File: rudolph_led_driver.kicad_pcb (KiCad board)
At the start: 2 copper layers, 96 x 23 mm, 33 parts, among them J1 Conn_01x02_Female, J2 USB_B_Micro, J3 Conn_01x02_Male, Q1 S8050, Q2 2SC1815, Q3 2SC1815, Q4 S8050, Q5 S8050, Q6 2SC1815, SW1 ON/OFF, U1 LM809, U2 LP2980-ADJ, U3 MCP73831-2-OT

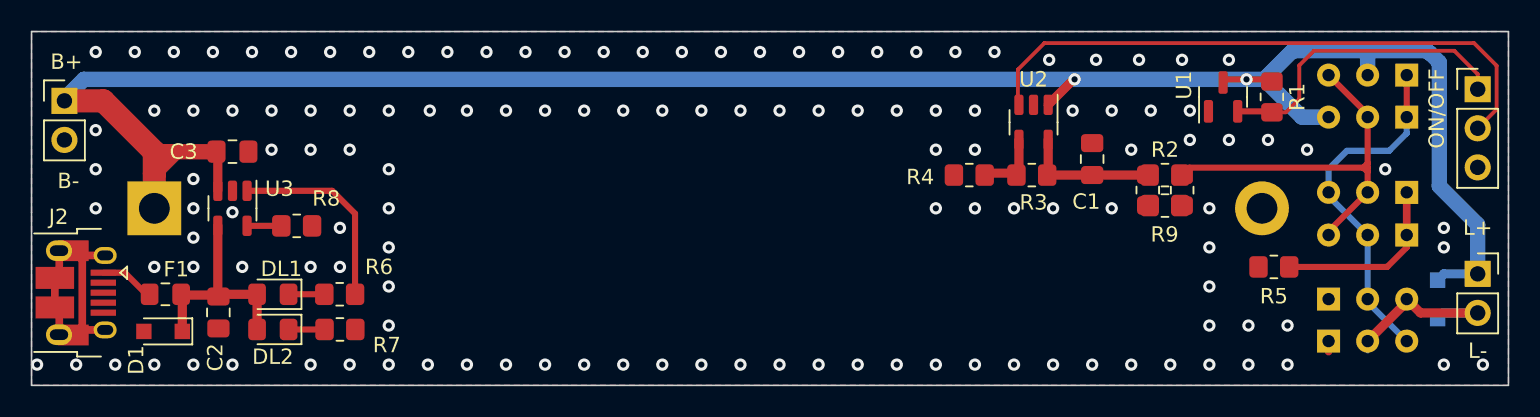
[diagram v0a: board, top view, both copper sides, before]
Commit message: Minor tweaks to the voltage reference generator
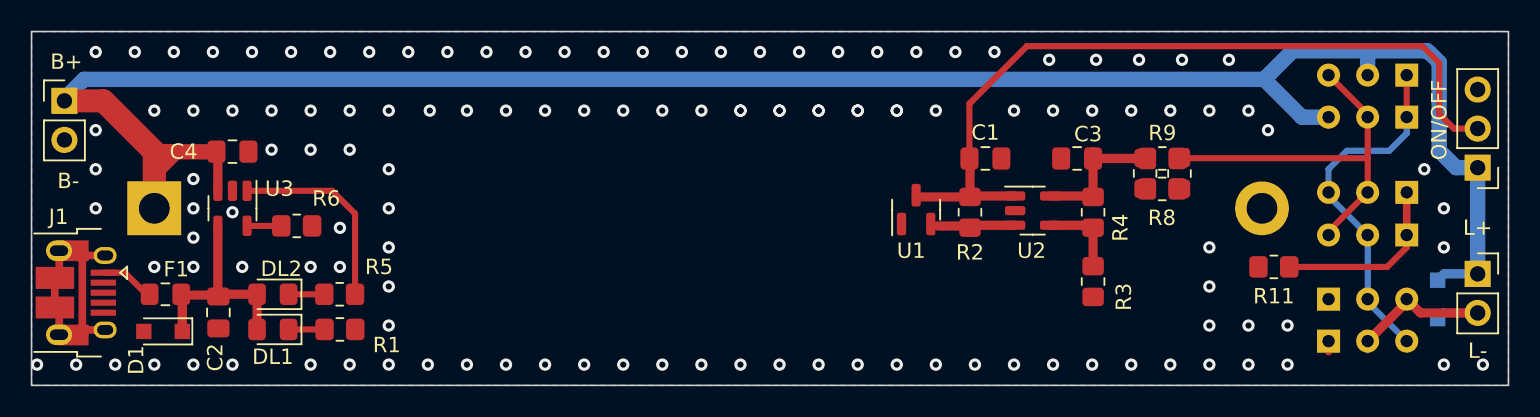
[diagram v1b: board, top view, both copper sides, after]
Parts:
- added C1: 4.7uF, Capacitor_SMD:C_0805_2012Metric_Pad1.18x1.45mm_HandSolder, F.Cu at (148.0, 75.5)
- C3: renamed from C1; value 2.2uF -> 4.7uF
- U1: value LM809 -> BD49K33G
- moved U1 21.3 mm to (143.5, 78.8)
- moved R2 21.0 mm to (147.0, 79.0)
- moved R3 10.6 mm to (155.0, 83.5), turned to -90 degrees
- moved U2 5.74 mm to (151.1, 78.9), turned to 0 degrees
- moved SW1 5.10 mm to (180.0, 76.1), turned to 180 degrees
- moved R4 4.66 mm to (155.0, 79.0), turned to 90 degrees
- moved R10 1.09 mm to (160.6, 76.5)
- moved R7 1.09 mm to (158.4, 76.5)
- moved R8 1.09 mm to (159.5, 77.5)
- moved R9 1.09 mm to (159.5, 75.5)
- moved C3 0.98 mm to (154.0, 75.5), turned to 180 degrees
- renumbered C3 to C4, DL2 to DL1, DL1 to DL2, J2 to J1, J1 to J2, Q3 to Q1, Q4 to Q2, Q1 to Q3, Q2 to Q4, R7 to R1, R11 to R10, R5 to R11, R1 to R2, R4 to R3, R3 to R4, R6 to R5, R8 to R6, R10 to R7, R9 to R8, R2 to R9
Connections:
- R2 pad 1: +BATT -> Net-(SW1-B)
- R2 pad 2: Net-(R1-Pad2) -> Net-(U1-~{RESET})
- SW1 pad 1: Net-(R1-Pad2) -> +BATT
- SW1 pad 2: Net-(SW1-Pad2) -> Net-(SW1-B)
- U1 pad 2: Net-(R1-Pad2) -> Net-(U1-~{RESET})
- U1 pad 3: +BATT -> Net-(SW1-B)
- U2 pad 1: +BATT -> Net-(SW1-B)
- U2 pad 3: Net-(SW1-Pad2) -> Net-(U1-~{RESET})
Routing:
- net Net-(SW1-B): track 0.00 -> 51.0 mm
- net Net-(SW1-Pad2): track 39.3 -> 0.00 mm
- net Net-(R1-Pad2): track 20.2 -> 0.00 mm
- net Net-(U1-~{RESET}): track 0.00 -> 5.06 mm
- net +BATT: track 142.2 -> 137.3 mm, vias 2 -> 0
- net Net-(U2-ADJ): track 4.00 -> 5.43 mm
- net /Vref_2V5: track 8.86 -> 9.44 mm
- net GND: vias 131 -> 126
